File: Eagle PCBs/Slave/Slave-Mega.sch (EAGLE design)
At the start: 11 parts, among them Q1 TIP120

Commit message: Minor PCB adjustments
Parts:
- R2: device rcl:R-EU_0204/7 -> rcl:R-EU_0207/10
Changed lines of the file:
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@@
 <grid distance="0.1" unitdist="inch" unit="inch" style="lines" multiple="1" display="no" altdistance="0.01" altunitdist="inch" altunit="inch"/>
 <layers>
-<layer number="1" name="Top" color="4" fill="1" visible="no" active="no"/>
-<layer number="16" name="Bottom" color="1" fill="1" visible="no" active="no"/>
-<layer number="17" name="Pads" color="2" fill="1" visible="no" active="no"/>
-<layer number="18" name="Vias" color="2" fill="1" visible="no" active="no"/>
-<layer number="19" name="Unrouted" color="6" fill="1" visible="no" active="no"/>
-<layer number="20" name="Dimension" color="24" fill="1" visible="no" active="no"/>
-<layer number="21" name="tPlace" color="7" fill="1" visible="no" active="no"/>
-<layer number="22" name="bPlace" color="7" fill="1" visible="no" active="no"/>
-<layer number="23" name="tOrigins" color="15" fill="1" visible="no" active="no"/>
-<layer number="24" name="bOrigins" color="15" fill="1" visible="no" active="no"/>
-<layer number="25" name="tNames" color="7" fill="1" visible="no" active="no"/>
-<layer number="26" name="bNames" color="7" fill="1" visible="no" active="no"/>
-<layer number="27" name="tValues" color="7" fill="1" visible="no" active="no"/>
-<layer number="28" name="bValues" color="7" fill="1" visible="no" active="no"/>
+<layer number="1" name="Top" color="4" fill="1" visible="yes" active="no"/>
+<layer number="16" name="Bottom" color="1" fill="1" visible="yes" active="no"/>
+<layer number="17" name="Pads" color="2" fill="1" visible="yes" active="no"/>
+<layer number="18" name="Vias" color="2" fill="1" visible="yes" active="no"/>
+<layer number="19" name="Unrouted" color="6" fill="1" visible="yes" active="no"/>
+<layer number="20" name="Dimension" color="24" fill="1" visible="yes" active="no"/>
+<layer number="21" name="tPlace" color="7" fill="1" visible="yes" active="no"/>
+<layer number="22" name="bPlace" color="7" fill="1" visible="yes" active="no"/>
+<layer number="23" name="tOrigins" color="15" fill="1" visible="yes" active="no"/>
+<layer number="24" name="bOrigins" color="15" fill="1" visible="yes" active="no"/>
+<layer number="25" name="tNames" color="7" fill="1" visible="yes" active="no"/>
+<layer number="26" name="bNames" color="7" fill="1" visible="yes" active="no"/>
+<layer number="27" name="tValues" color="7" fill="1" visible="yes" active="no"/>
+<layer number="28" name="bValues" color="7" fill="1" visible="yes" active="no"/>
 <layer number="29" name="tStop" color="7" fill="3" visible="no" active="no"/>
 <layer number="30" name="bStop" color="7" fill="6" visible="no" active="no"/>
@@
 <layer number="35" name="tGlue" color="7" fill="4" visible="no" active="no"/>
 <layer number="36" name="bGlue" color="7" fill="5" visible="no" active="no"/>
-<layer number="37" name="tTest" color="7" fill="1" visible="no" active="no"/>
-<layer number="38" name="bTest" color="7" fill="1" visible="no" active="no"/>
+<layer number="37" name="tTest" color="7" fill="1" visible="yes" active="no"/>
+<layer number="38" name="bTest" color="7" fill="1" visible="yes" active="no"/>
 <layer number="39" name="tKeepout" color="4" fill="11" visible="no" active="no"/>
 <layer number="40" name="bKeepout" color="1" fill="11" visible="no" active="no"/>
@@
 <layer number="44" name="Drills" color="7" fill="1" visible="no" active="no"/>
 <layer number="45" name="Holes" color="7" fill="1" visible="no" active="no"/>
-<layer number="46" name="Milling" color="3" fill="1" visible="no" active="no"/>
-<layer number="47" name="Measures" color="7" fill="1" visible="no" active="no"/>
-<layer number="48" name="Document" color="7" fill="1" visible="no" active="no"/>
-<layer number="49" name="Reference" color="7" fill="1" visible="no" active="no"/>
-<layer number="50" name="dxf" color="7" fill="1" visible="no" active="no"/>
-<layer number="51" name="tDocu" color="7" fill="1" visible="no" active="no"/>
-<layer number="52" name="bDocu" color="7" fill="1" visible="no" active="no"/>
-<layer number="53" name="tGND_GNDA" color="7" fill="9" visible="no" active="no"/>
-<layer number="54" name="bGND_GNDA" color="1" fill="9" visible="no" active="no"/>
-<layer number="56" name="wert" color="7" fill="1" visible="no" active="no"/>
+<layer number="46" name="Milling" color="3" fill="1" visible="yes" active="no"/>
+<layer number="47" name="Measures" color="7" fill="1" visible="yes" active="no"/>
+<layer number="48" name="Document" color="7" fill="1" visible="yes" active="no"/>
+<layer number="49" name="Reference" color="7" fill="1" visible="yes" active="no"/>
+<layer number="50" name="dxf" color="7" fill="1" visible="yes" active="no"/>
+<layer number="51" name="tDocu" color="7" fill="1" visible="yes" active="no"/>
+<layer number="52" name="bDocu" color="7" fill="1" visible="yes" active="no"/>
+<layer number="53" name="tGND_GNDA" color="7" fill="9" visible="yes" active="no"/>
+<layer number="54" name="bGND_GNDA" color="1" fill="9" visible="yes" active="no"/>
+<layer number="56" name="wert" color="7" fill="1" visible="yes" active="no"/>
 <layer number="88" name="SimResults" color="9" fill="1" visible="yes" active="yes"/>
 <layer number="89" name="SimProbes" color="9" fill="1" visible="yes" active="yes"/>
@@
 <part name="TERM" library="pinhead" library_urn="urn:adsk.eagle:library:325" deviceset="PINHD-1X2" device="" package3d_urn="urn:adsk.eagle:package:22435/2"/>
 <part name="R1" library="rcl" library_urn="urn:adsk.eagle:library:334" deviceset="R-EU_" device="0204/7" package3d_urn="urn:adsk.eagle:package:23498/2" value="120Ω"/>
-<part name="R2" library="rcl" library_urn="urn:adsk.eagle:library:334" deviceset="R-EU_" device="0204/7" package3d_urn="urn:adsk.eagle:package:23498/2" value="1K"/>
+<part name="R2" library="rcl" library_urn="urn:adsk.eagle:library:334" deviceset="R-EU_" device="0207/10" package3d_urn="urn:adsk.eagle:package:23491/2" value="1K"/>
 <part name="Q1" library="transistor-power" library_urn="urn:adsk.eagle:library:400" deviceset="TIP120" device="" package3d_urn="urn:adsk.eagle:package:29488/1"/>
 <part name="LED" library="con-molex" library_urn="urn:adsk.eagle:library:165" deviceset="KK-156-2" device="" package3d_urn="urn:adsk.eagle:package:8078800/1"/>

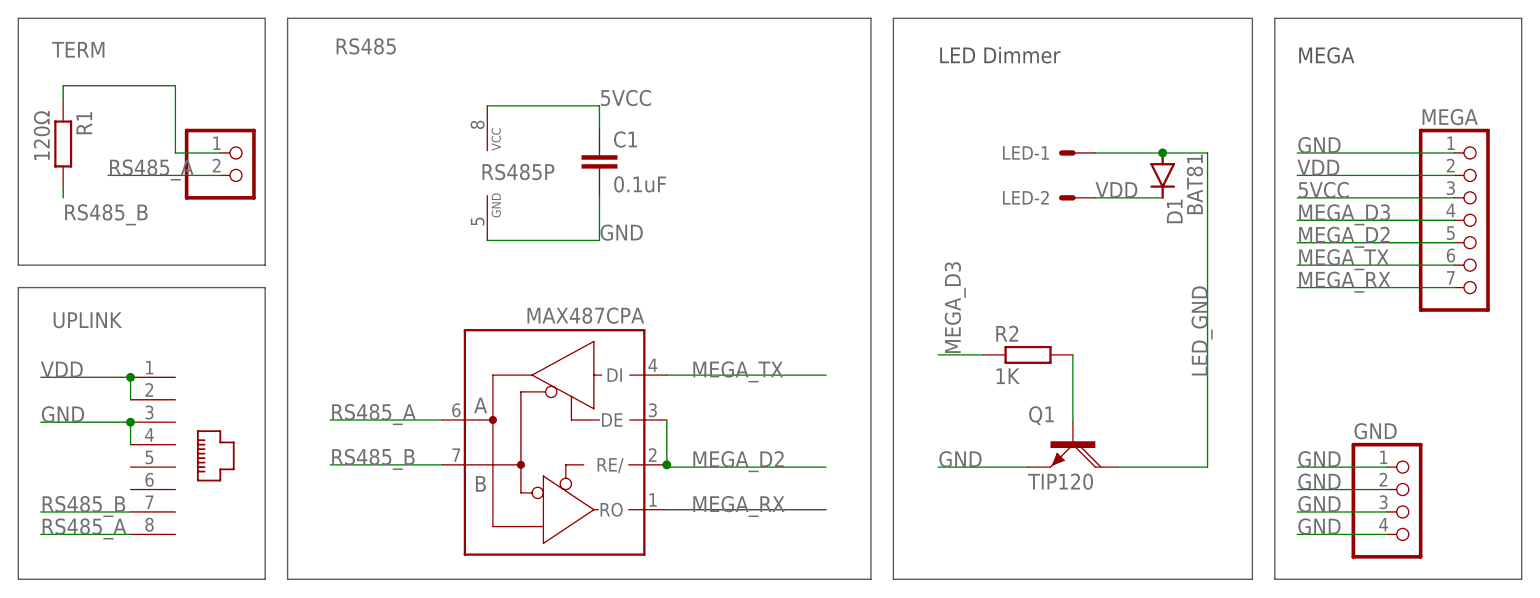
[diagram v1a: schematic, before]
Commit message: Added a 5v bus to all PCBs
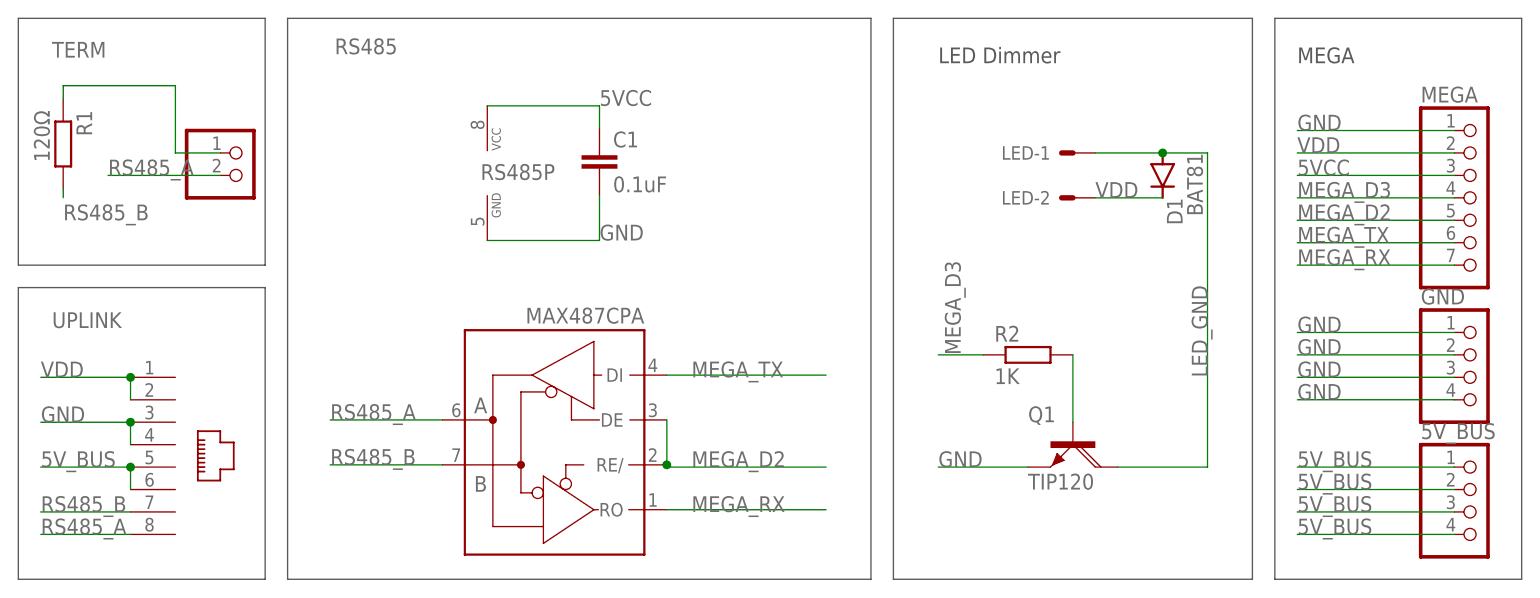
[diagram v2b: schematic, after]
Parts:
- added 5V_BUS: (no value), pinhead:PINHD-1X4
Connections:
- new net 5V_BUS: 5V_BUS.1, 5V_BUS.2, 5V_BUS.3, 5V_BUS.4, UPLINK.5, UPLINK.6
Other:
- moved on the sheet: GND, MEGA
